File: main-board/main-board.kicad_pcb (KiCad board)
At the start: 2 copper layers, 64 parts, among them J1 NVIDIA_Jetson_NX_Dev_40pin_Co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, J10 FSESC_6.6_COMM, J11 FSESC_6.6_COMM, J12 FSESC_6.6_COMM, J13 FSESC_6.6_COMM, J2 NVIDIA_Jetson_NX_Dev_Button_C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, J3 Conn_01x02, J4 Conn_01x02, J5 Conn_01x02, J6 QWIIC_Generic_Conn, J7 Conn_01x03, J8 FSESC_6.6_COMM, J9 FSESC_6.6_COMM, M1 Fan_3pin, M2 Fan_3pin, M3 Fan_3pin, Q1 Q_NMOS_GSD, Q2 Q_NMOS_GSD, Q3 Q_NMOS_GSD, Q4 Q_NMOS_GSD, Q5 Q_NMOS_GSD, Q6 Q_NMOS_GSD, Q7 Q_NMOS_GSD, U1 RFM95W_Adafruit_Breakout, U10 Adafruit_GPS_V3, U12 SN74AHCT125D, U2 TDK_I3A4W008A033V, U3 TDK_I3A4W008A033V, U4 Teensy_4.1, U5 Analog Temp Sensor, U6 Analog Temp Sensor, U7 Analog Temp Sensor, U8 Analog Temp Sensor, U9 Analog Temp Sensor

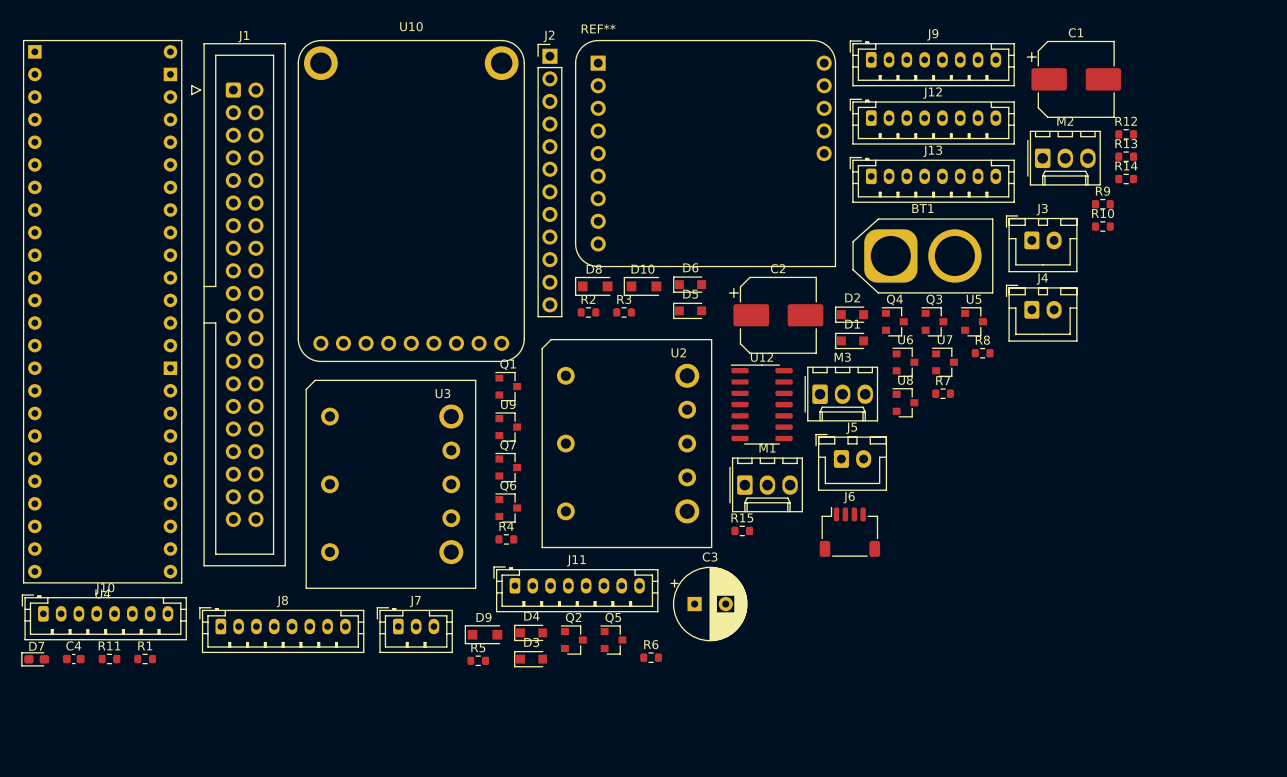
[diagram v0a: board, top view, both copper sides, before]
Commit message: 24v power supply swapped
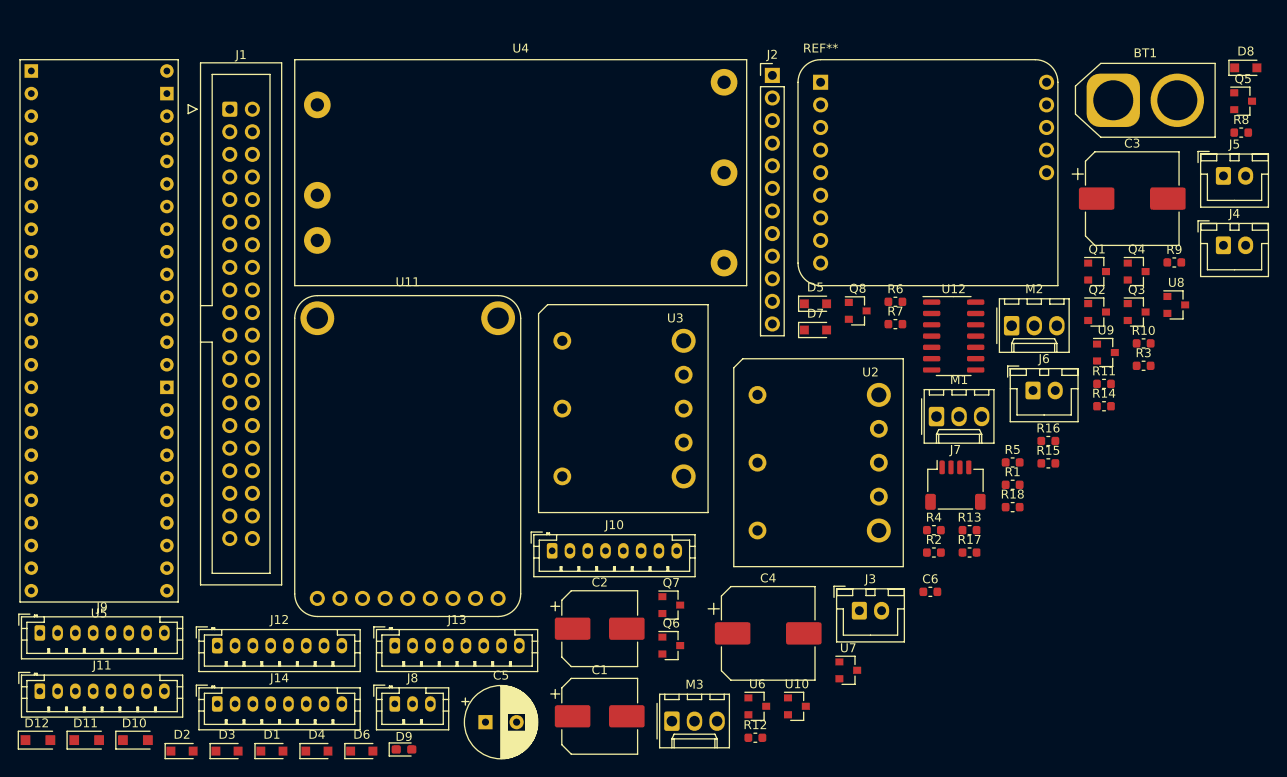
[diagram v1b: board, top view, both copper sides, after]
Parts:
- added C5: 1000u, Capacitor_THT:CP_Radial_D8.0mm_P3.50mm, F.Cu at (71.4, 95.4)
- added C6: 100n, Capacitor_SMD:C_0603_1608Metric, F.Cu at (121.4, 80.8)
- added D11: D_Schottky_Small, Diode_SMD:D_SOD-123F, F.Cu at (26.6, 97.4)
- added D12: D_Schottky_Small, Diode_SMD:D_SOD-123F, F.Cu at (21.1, 97.4)
- added J14: FSESC_6.6_COMM, Connector_JST:JST_PH_B8B-PH-K_1x08_P2.00mm_Vertical, F.Cu at (41.3, 93.3)
- added Q8: Q_NMOS_GSD, Package_TO_SOT_SMD:SOT-23, F.Cu at (113.3, 49.2)
- added R16: 10k, Resistor_SMD:R_0603_1608Metric, F.Cu at (134.7, 63.8)
- added R17: 10k, Resistor_SMD:R_0603_1608Metric, F.Cu at (125.8, 76.3)
- added R18: 10k, Resistor_SMD:R_0603_1608Metric, F.Cu at (130.7, 71.2)
- added U11: Adafruit_GPS_V3, ASTRA_Footprints:Adafruit_GPS_Breakout, F.Cu at (62.7, 81.5)
- C3: value 1000u -> 100u; footprint Capacitor_THT:CP_Radial_D8.0mm_P3.50mm -> Capacitor_SMD:CP_Elec_10x10
- C4: value 100n -> 100u; footprint Capacitor_SMD:C_0603_1608Metric -> Capacitor_SMD:CP_Elec_10x10
- D7: value LED -> D_Schottky_Small; footprint LED_SMD:LED_0603_1608Metric_Pad1.05x0.95mm_HandSolder -> Diode_SMD:D_SOD-323_HandSoldering
- D8: footprint Diode_SMD:D_SOD-123F -> Diode_SMD:D_SOD-323_HandSoldering
- D9: value D_Schottky_Small -> LED; footprint Diode_SMD:D_SOD-123F -> LED_SMD:LED_0603_1608Metric_Pad1.05x0.95mm_HandSolder
- J6: value QWIIC_Generic_Conn -> Conn_01x02; footprint Connector_JST:JST_SH_SM04B-SRSS-TB_1x04-1MP_P1.00mm_Horizontal -> Connector_JST:JST_XH_B2B-XH-A_1x02_P2.50mm_Vertical
- J7: value Conn_01x03 -> QWIIC_Generic_Conn; footprint Connector_JST:JST_PH_B3B-PH-K_1x03_P2.00mm_Vertical -> Connector_JST:JST_SH_SM04B-SRSS-TB_1x04-1MP_P1.00mm_Horizontal
- J8: value FSESC_6.6_COMM -> Conn_01x03; footprint Connector_JST:JST_PH_B8B-PH-K_1x08_P2.00mm_Vertical -> Connector_JST:JST_PH_B3B-PH-K_1x03_P2.00mm_Vertical
- R10, R12, R6, R8: value 10k -> 80.6k
- R3: value 1.82k -> 100k
- R4: value 8.45k -> 1.82k
- R5: value 80.6k -> 8.45k
- R7, R9: value 80.6k -> 10k
- U10: value Adafruit_GPS_V3 -> Analog Temp Sensor; footprint ASTRA_Footprints:Adafruit_GPS_Breakout -> Package_TO_SOT_SMD:SOT-23
- U4: value Teensy_4.1 -> PYBE30-Q24-S24; footprint ASTRA_Footprints:Teensy4.1 -> ASTRA_Footprints:PYBE30
- U5: value Analog Temp Sensor -> Teensy_4.1; footprint Package_TO_SOT_SMD:SOT-23 -> ASTRA_Footprints:Teensy4.1
- moved R11 116.0 mm to (141.0, 57.4)
- moved J9 113.5 mm to (21.3, 85.4)
- moved U5 111.8 mm to (19.1, 81.9)
- moved R1 99.5 mm to (130.7, 68.7)
- moved D7 95.1 mm to (108.5, 51.3)
- moved J12 94.4 mm to (41.3, 86.8)
- moved Q5 93.2 mm to (156.6, 25.6)
- moved D2 89.9 mm to (37.3, 98.7)
- moved C1 89.4 mm to (84.3, 94.7)
- moved D1 79.9 mm to (47.4, 98.7)
- moved R12 79.6 mm to (101.8, 97.2)
- moved C4 78.1 mm to (103.2, 85.4)
- moved D8 77.2 mm to (156.9, 21.9)
- moved D10 76.6 mm to (32.1, 97.4)
- moved J13 75.2 mm to (61.2, 86.8)
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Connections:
- C3 pad 1: +5V -> +BATT
- C4 pad 1: +5V -> +24V
- D5 pad 2: /ADC_5V -> /ADC_24V
- D6 pad 1: /ADC_5V -> /ADC_24V
- D7 pad 1: Net-(D7-Pad1) -> +3V3
- D7 pad 2: Net-(D7-Pad2) -> /ADC_5V
- D8 pad 1: +12V -> /ADC_5V
- D8 pad 2: Net-(D8-Pad2) -> GND
- D9 pad 1: +12V -> Net-(D9-Pad1)
- J10 pad 5: /M3_RX -> /M2_RX
- J10 pad 6: /M3_TX -> /M2_TX
- J11 pad 5: /M4_RX -> /M3_RX
- J11 pad 6: /M4_TX -> /M3_TX
- J12 pad 5: /M5_RX -> /M4_RX
- J12 pad 6: /M5_TX -> /M4_TX
- J13 pad 5: /M6_RX -> /M5_RX
- J13 pad 6: /M6_TX -> /M5_TX
- J2 pad 1: Net-(D7-Pad1) -> Net-(D9-Pad1)
- J2 pad 2: Net-(D7-Pad2) -> Net-(D9-Pad2)
- J6 pad 1: GND -> +24V
- J6 pad 2: +3V3 -> GND
- J7 pad 1: +5V -> GND
- J7 pad 2: GND -> +3V3
- J7 pad 3: Net-(J7-Pad3) -> /NX_SDA
- J8 pad 1: Net-(J8-Pad1) -> +5V
- J8 pad 2: Net-(J8-Pad2) -> GND
- J8 pad 3: GND -> Net-(J8-Pad3)
- J9 pad 5: /M2_RX -> /M1_RX
- J9 pad 6: /M2_TX -> /M1_TX
- M1 pad 1: Net-(D8-Pad2) -> Net-(D10-Pad2)
- M2 pad 1: Net-(D9-Pad2) -> Net-(D11-Pad2)
- M3 pad 1: Net-(D10-Pad2) -> Net-(D12-Pad2)
- Q3 pad 1: /JETSON_RESET -> /24V_Disable
- Q3 pad 3: Net-(J2-Pad8) -> Net-(Q3-Pad3)
- Q4 pad 1: /JETSON_SLEEP -> /JETSON_RESET
- Q4 pad 3: Net-(J2-Pad12) -> Net-(J2-Pad8)
- Q5 pad 1: /Fan1_Control -> /JETSON_SLEEP
- Q5 pad 3: Net-(D8-Pad2) -> Net-(J2-Pad12)
- Q6 pad 1: /Fan2_Control -> /Fan1_Control
- Q6 pad 3: Net-(D9-Pad2) -> Net-(D10-Pad2)
- Q7 pad 1: /Fan3_Control -> /Fan2_Control
- Q7 pad 3: Net-(D10-Pad2) -> Net-(D11-Pad2)
- R10 pad 1: /ADC_5V -> +24V
- R10 pad 2: GND -> /ADC_24V
- R11 pad 1: /JETSON_RESET -> /ADC_24V
- R12 pad 1: /JETSON_SLEEP -> +5V
- R12 pad 2: GND -> /ADC_5V
- R13 pad 1: /Fan1_Control -> /ADC_5V
- R14 pad 1: /Fan2_Control -> /JETSON_RESET
- R15 pad 1: /Fan3_Control -> /JETSON_SLEEP
- R3 pad 1: +12V -> /24V_Disable
- R3 pad 2: Net-(R3-Pad2) -> GND
- R4 pad 1: +5V -> +12V
- R5 pad 1: +BATT -> +5V
- R5 pad 2: /ADC_BATT -> Net-(R5-Pad2)
- R6 pad 1: /ADC_BATT -> +BATT
- R6 pad 2: GND -> /ADC_BATT
- R7 pad 1: +12V -> /ADC_BATT
- R7 pad 2: /ADC_12V -> GND
- R8 pad 1: /ADC_12V -> +12V
- R8 pad 2: GND -> /ADC_12V
- R9 pad 1: +5V -> /ADC_12V
- R9 pad 2: /ADC_5V -> GND
- U10 pad 1: Net-(U10-Pad1) -> +3V3
- U10 pad 2: Net-(U10-Pad2) -> /ADC5
- U10 pad 3: Net-(U10-Pad3) -> GND
- U12 pad 3: Net-(J7-Pad3) -> Net-(J8-Pad3)
- U2 pad 6: Net-(R3-Pad2) -> Net-(R4-Pad2)
- U3 pad 6: Net-(R4-Pad2) -> Net-(R5-Pad2)
- U4 pad 1: GND -> +BATT
- U4 pad 2: /M1_RX -> GND
- U4 pad 3: /M1_TX -> Net-(Q3-Pad3)
- U4 pad 4: /ARGB_Data -> Net-(U4-Pad4)
- U4 pad 5: /COMMS_RST -> GND
- U4 pad 6: /COMMS_G0 -> +24V
- U5 pad 1: +3V3 -> GND
- U5 pad 2: /ADC1 -> /M1_RX
- U5 pad 3: GND -> /M1_TX
- U6 pad 2: /ADC2 -> /ADC1
- U7 pad 2: /ADC3 -> /ADC2
- U8 pad 2: /ADC4 -> /ADC3
- U9 pad 2: /ADC5 -> /ADC4

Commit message: Update main-board.kicad_pcb
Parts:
- moved U4 351.2 mm to (421.1, 95.2)
- moved C4 349.8 mm to (452.6, 102.6), turned to 90 degrees
- moved U3 349.3 mm to (429.3, 61.2)
- moved C1 341.2 mm to (420.1, 34.3), turned to 180 degrees
- moved C2 336.5 mm to (419.9, 60.5), turned to 180 degrees
- moved U2 328.1 mm to (429.3, 35.1)
- moved R4 327.9 mm to (447.5, 35.8), turned to 270 degrees
- moved R5 317.1 mm to (447.8, 62.0), turned to 270 degrees
- moved R2 300.8 mm to (422.7, 73.4), turned to 270 degrees
- moved BT1 297.2 mm to (432.8, -35.6), turned to 180 degrees
- moved R1 292.8 mm to (422.7, 47.2), turned to 270 degrees
- moved J13 287.7 mm to (347.7, 112.8)
- moved Q2 284.2 mm to (423.7, 69.8), turned to 90 degrees
- moved Q1 283.5 mm to (423.7, 43.7), turned to 90 degrees
- moved U1 282.0 mm to (385.3, -33.3)
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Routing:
- net /NX_SDA: track 0.00 -> 55.0 mm
- net /NX_SCL: track 0.00 -> 52.3 mm
- net GND: track 0.00 -> 32.5 mm
- net +5V: track 0.00 -> 19.4 mm
- net +3V3: track 0.00 -> 16.8 mm, vias 0 -> 1
- net +BATT: track 0.00 -> 16.6 mm
- net +12V: track 0.00 -> 14.7 mm
- net /ADC_5V: track 0.00 -> 11.1 mm
- net /ADC_BATT: track 0.00 -> 10.9 mm
- net /ADC_12V: track 0.00 -> 10.9 mm
- net /ADC_24V: track 0.00 -> 10.9 mm
- net Net-(J8-Pad3): track 0.00 -> 9.97 mm
- net +24V: track 0.00 -> 9.14 mm
- net Net-(D12-Pad2): track 0.00 -> 8.64 mm
- net Net-(D11-Pad2): track 0.00 -> 8.64 mm
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
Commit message: pcb layout attempt
Tried to squish stuff together while still leaving room for traces (probably really rough)
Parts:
- moved U1 347.0 mm to (58.2, 82.5), turned to 90 degrees
- moved C4 326.0 mm to (126.7, 94.7)
- moved BT1 325.1 mm to (120.5, 54.6)
- moved J10 302.9 mm to (45.2, 119.6)
- moved J13 302.8 mm to (45.2, 125.5)
- moved J12 296.1 mm to (25.9, 125.5)
- moved C2 289.0 mm to (131.6, 80.3)
- moved Q1 289.0 mm to (135.4, 63.5)
- moved Q2 289.0 mm to (135.4, 89.7)
- moved Q3 289.0 mm to (105.2, 108.5)
- moved R3 289.0 mm to (104.1, 112.0)
- moved R5 289.0 mm to (159.5, 81.8)
- moved C1 289.0 mm to (131.8, 54.1)
- moved C3 289.0 mm to (101.6, 122.4)
- moved R1 289.0 mm to (134.4, 67.1)
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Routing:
- net +24V: track 9.14 -> 41.6 mm
- net /NX_SDA: track 55.0 -> 35.7 mm
- net /NX_SCL: track 52.3 -> 42.9 mm
